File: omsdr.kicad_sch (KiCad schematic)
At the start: 54 parts, among them J1 I/Q Out, J2 ANT, J3 ISP, J4 LO, J5 I/Q Out, J8 IO, SW1 LEFT, SW2 RIGHT, T1 CX2074NL, U1 LT6231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

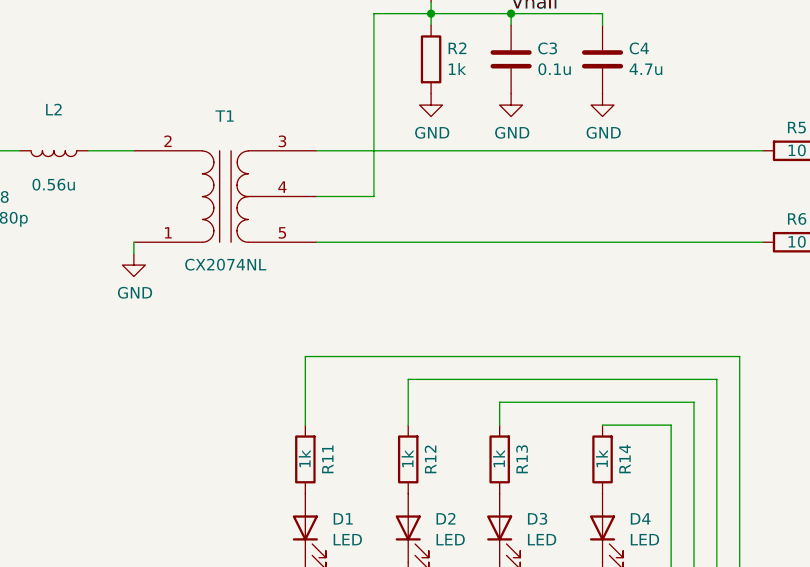
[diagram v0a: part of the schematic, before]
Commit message: Replacing wrong balun with correct part
We used some 1:4 part, but we really should use a 1:1 part with
center tap. Otherwise the impedance seen when looking into the
atenna port will be way off. What we really need to see is the
sampling cap (a short to GND at RF frequencies), followed by the
internal switch resistance (5 ish Ohm or so?), followed by the
10 Ohm series resistor, i.e. a total of 15ish Ohm multiplied by
4 (60 Ohm). If we use a 1:1 transformer, then one secondary winding from
the center tap to the end has half the turns of the primary side;
a turns ratio of 2:1 yields an impedance ratio of 4:1 which is
what we are looking for.
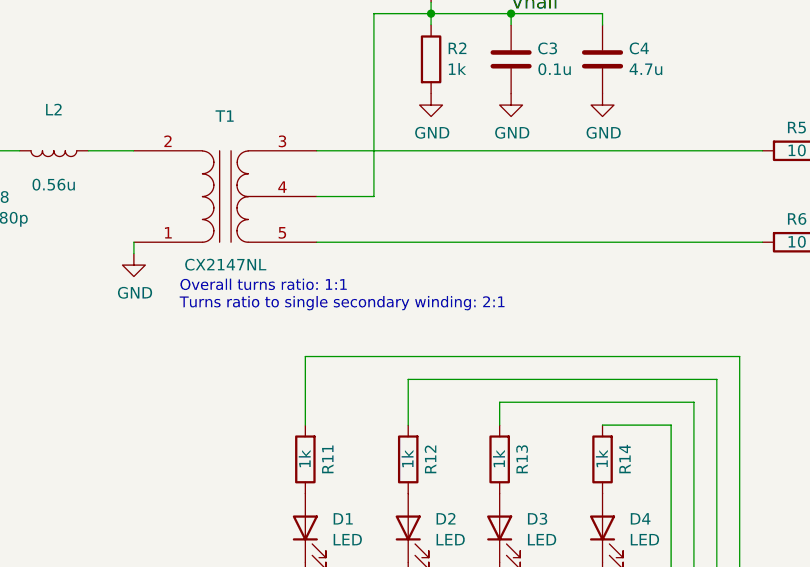
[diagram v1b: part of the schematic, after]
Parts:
- T1: value CX2074NL -> CX2147NL; BOM DIST DIGIKEY 553-1655-ND -> DIST DIGIKEY 553-1501-ND
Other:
- note added: "Overall turns ratio: 1:1 Turns ratio to single secondary winding: 2:1"
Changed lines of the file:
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@@
     (effects (font (size 5.0038 5.0038) (thickness 1.0008) bold) (justify left bottom))
+  )
+  (text "Overall turns ratio: 1:1\nTurns ratio to single secondary winding: 2:1"
+    (at 78.74 80.01 0)
+    (effects (font (size 1.2 1.2)) (justify left bottom))
   )
   (text "Design by Matt Weyland (HB9FRV)\n\nBased on work by Tony Parks\n(c) 2017,18,19,22 CC-BY-SA"
@@
     (in_bom yes) (on_board yes)
     (property "Reference" "T1" (id 0) (at 83.82 58.42 0))
-    (property "Value" "CX2074NL" (id 1) (at 83.82 74.93 0))
+    (property "Value" "CX2147NL" (id 1) (at 83.82 74.93 0))
     (property "Footprint" "local:CX2074" (id 2) (at 83.82 67.31 0)
       (effects (font (size 1.27 1.27)) hide)
@@
       (effects (font (size 1.27 1.27)) hide)
     )
-    (property "BOM" "DIST DIGIKEY  553-1655-ND" (id 4) (at 83.82 67.31 0)
+    (property "BOM" "DIST DIGIKEY 553-1501-ND" (id 4) (at 83.82 67.31 0)
       (effects (font (size 1.524 1.524)) hide)
     )
@@
     )
     (path "/00000000-0000-0000-0000-00005a04a23a"
-      (reference "T1") (unit 1) (value "CX2074NL") (footprint "local:CX2074")
+      (reference "T1") (unit 1) (value "CX2147NL") (footprint "local:CX2074")
     )
     (path "/0bfea883-37c1-4f77-b14d-494b066fd38f"
